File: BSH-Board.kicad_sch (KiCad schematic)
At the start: 25 parts, among them J1 667101210103, J30 MICRO QTZB5.0, SW1 TS-3025-B-C-B, SW2 TS-3025-B-C-B, U1 NCP715SQ50T2G, U2 ESP32-C6-MINI-1-N4, U3 TXS0102DQER, U5 AP63203WU

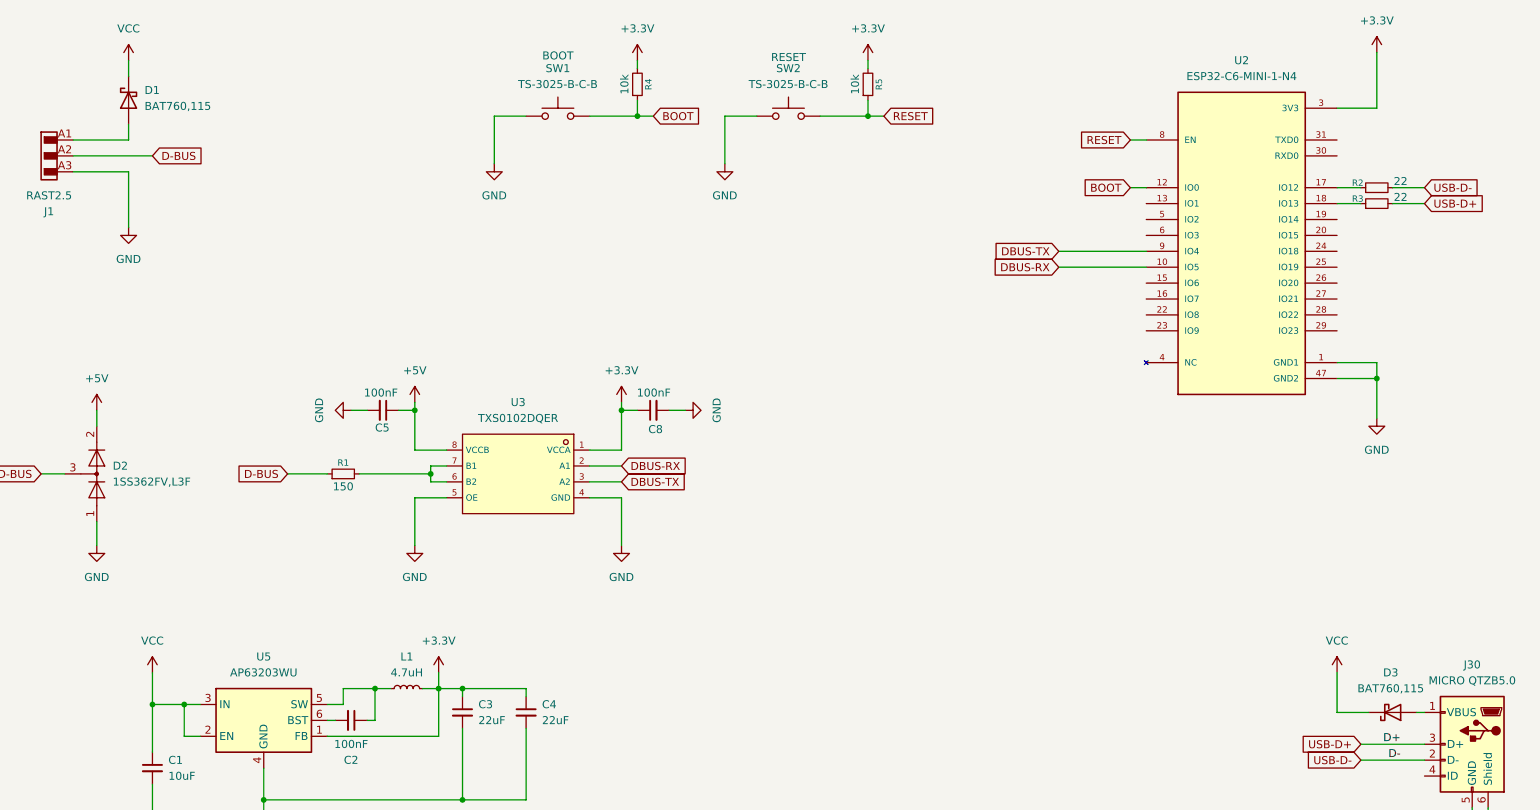
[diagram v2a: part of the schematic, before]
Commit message: Added LCSC numbers, replaced parts with Basic parts, added LEDs
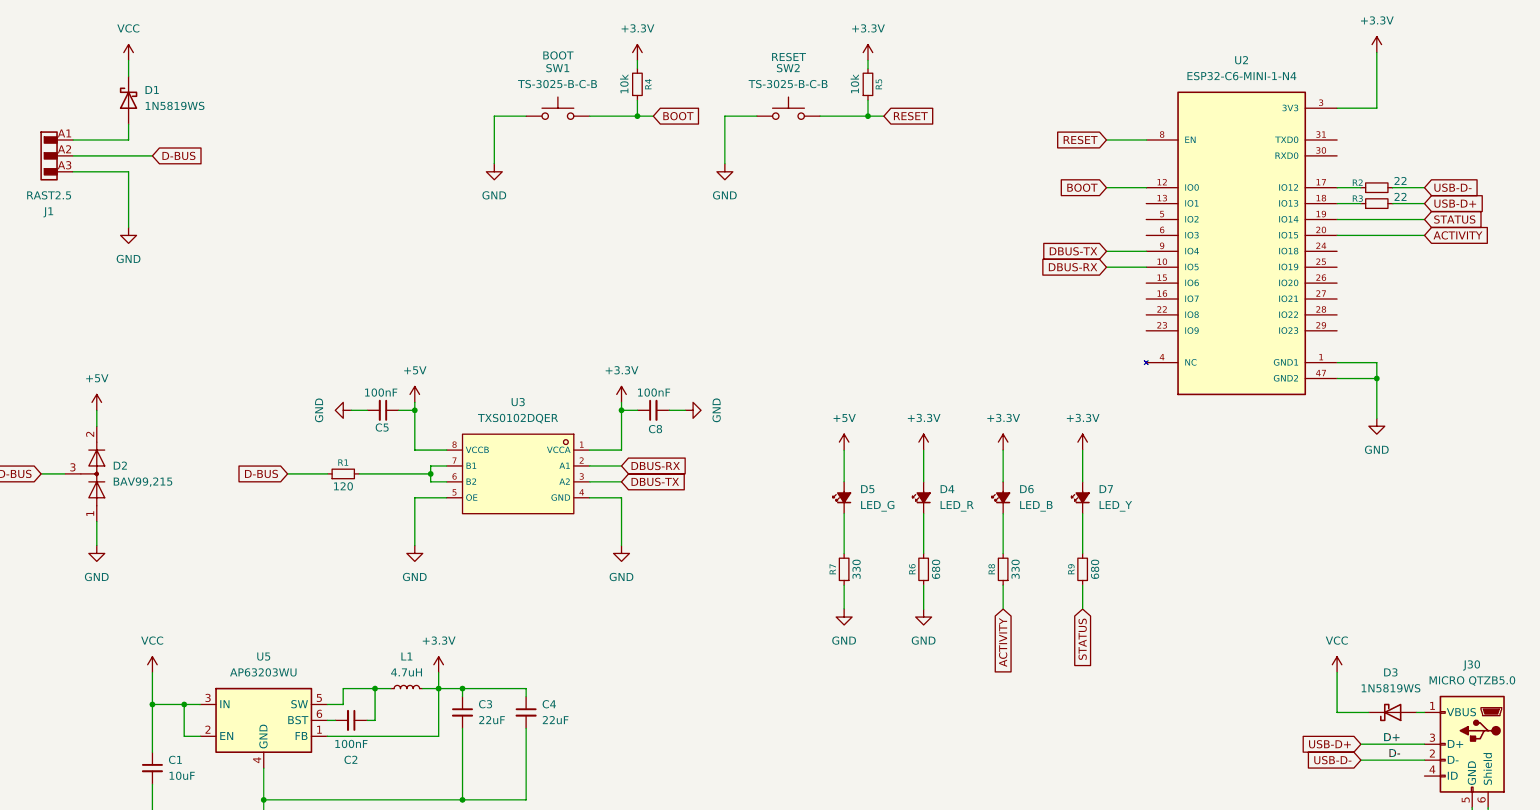
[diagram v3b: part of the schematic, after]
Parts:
- added D4: LED_R, LED_SMD:LED_0402_1005Metric, symbol Device:LED_Small_Filled
- added D5: LED_G, LED_SMD:LED_0402_1005Metric, symbol Device:LED_Small_Filled
- added D6: LED_B, LED_SMD:LED_0402_1005Metric, symbol Device:LED_Small_Filled
- added D7: LED_Y, LED_SMD:LED_0402_1005Metric, symbol Device:LED_Small_Filled
- added R6, R9: 680, Resistor_SMD:R_0402_1005Metric, symbol Device:R_Small
- added R7, R8: 330, Resistor_SMD:R_0402_1005Metric, symbol Device:R_Small
- C1: LCSC C15850 -> C96446
- C2: footprint Capacitor_SMD:C_0805_2012Metric -> Capacitor_SMD:C_0402_1005Metric; LCSC C14663 -> C307331
- C5, C8: LCSC C1525 -> C307331
- D1, D3: value BAT760,115 -> 1N5819WS; LCSC C117941 -> C191023; MPN BAT760,115 -> (none)
- D2: value 1SS362FV,L3F -> BAV99,215; footprint Package_TO_SOT_SMD:SOT-723 -> Package_TO_SOT_SMD:SOT-23
- R1: value 150 -> 120; LCSC (none) -> C25079
- R2, R3: LCSC (none) -> C25092
- R4, R5: LCSC (none) -> C25744
- SW1, SW2: LCSC (none) -> C2689695
- U2: LCSC (none) -> C5736265; MF Espressif Systems -> (none); MP ESP32-C6-MINI-1-N4 -> (none)
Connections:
- net +3.3V: now also D4.2 (A), D6.2 (A), D7.2 (A)
- net +5V: now also D5.2 (A)
- net GND: now also R6.1, R7.1
- net STATUS: now reaches U2.19 (IO14)
- net STATUS: now also R9.1
- net ACTIVITY: now reaches U2.20 (IO15)
- net ACTIVITY: now also R8.1
- new net: D6.1 (K), R8.2
- new net: D5.1 (K), R7.2
- new net: D7.1 (K), R9.2
- new net: D4.1 (K), R6.2

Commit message: Minor improvements
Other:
- moved on the sheet: C1, C2, C3, C4, C5, C6, C7, C8, D2, D3, D4, D5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

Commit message: Clenaupo
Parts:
- added C10, C9: 100nF, Capacitor_SMD:C_0402_1005Metric, symbol Device:C_Small
- L1: value 4.7uH -> 3.3uH; LCSC C5832360 -> C5832373
- renumbered C6 to C5, C7 to C6, C5 to C7, D5 to D6, D4 to D7, D7 to D8, D6 to D9, J30 to J2, R7 to R6, R6 to R7, R9 to R8, R8 to R9, SW2 to SW1, SW1 to SW2, U2 to U1, U5 to U2, U1 to U3, U3 to U4
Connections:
- net +3.3V: now also U4.8 (VCCB); no longer U4.1 (VCCA)
- net +5V: now also U4.1 (VCCA); no longer U4.8 (VCCB)
- net ACTIVITY: now also U1.16 (IO7); no longer U1.20 (IO15)
- net BOOT: now also U1.23 (IO9), C9.1; no longer U1.12 (IO0)
- net DBUS-RX: now also U1.9 (IO4), U4.7 (B1); no longer U1.10 (IO5), U4.2 (A1)
- net DBUS-TX: now also U1.10 (IO5), U4.6 (B2); no longer U1.9 (IO4), U4.3 (A2)
- net GND: now also C10.2, C9.2; no longer U4.5 (OE)
- net RESET: now also C10.1
- net STATUS: now also U1.15 (IO6); no longer U1.19 (IO14)
- new net: R1.2, U4.2 (A1), U4.3 (A2)
- new net DBUS-ENABLE: U1.12 (IO0), U4.5 (OE)
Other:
- company: (none) -> Bouni
- title: (none) -> BSH Board
- moved on the sheet: C3, C4, C5, C6, D3, D8, D9, J2, L1, R4, R8, R9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
